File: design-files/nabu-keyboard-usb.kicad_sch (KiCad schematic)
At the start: 15 parts, among them J1 Console UART header, J2 DIN-6, J3 9V input, Q1 IRLU110PBF, U1 74LVC245, U2 Pico, U3 SN75176AP

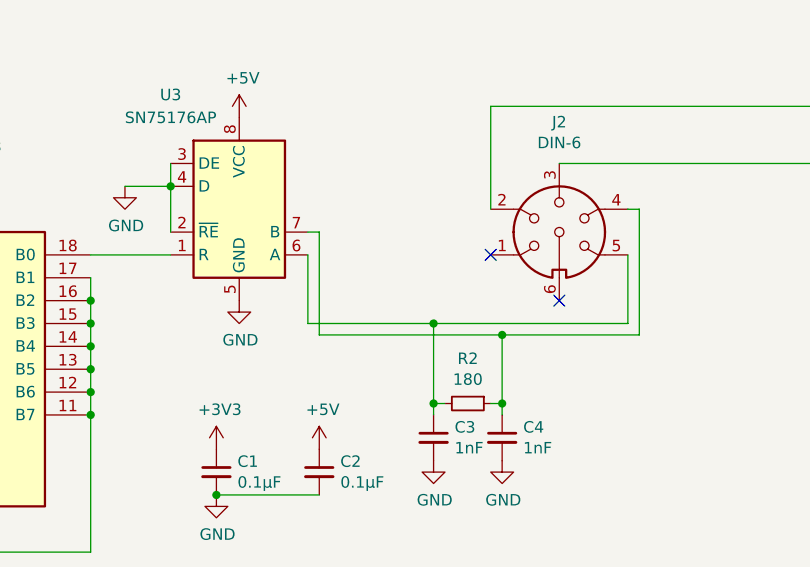
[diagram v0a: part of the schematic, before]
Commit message: Fix an error in the schematic that resulted in a non-working PCB; TX+ and TX- were swapped going into the 75176.
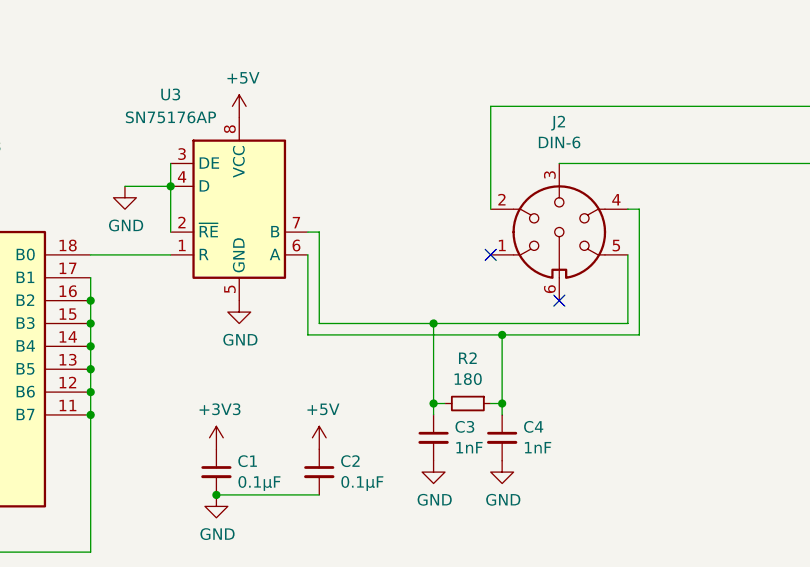
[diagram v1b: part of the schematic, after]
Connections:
- net at C3.1, J2.5, R2.2: now also U3.7 (B); no longer U3.6 (A)
- net at C4.1, J2.4, R2.1: now also U3.6 (A); no longer U3.7 (B)
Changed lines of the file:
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@@
   (title_block
     (title "NABU Keyboard to USB Adapter")
-    (date "2022-12-19")
-    (rev "0.1")
+    (date "2023-04-09")
+    (rev "0.2")
     (company "(c) 2022 Jason R. Thorpe. See LICENSE.")
   )
@@
   (junction (at 214.63 66.04) (diameter 0) (color 0 0 0 0)
   )
+  (junction (at 171.45 133.35) (diameter 0) (color 0 0 0 0)
+  )
   (junction (at 125.73 134.62) (diameter 0) (color 0 0 0 0)
   )
   (junction (at 125.73 129.54) (diameter 0) (color 0 0 0 0)
   )
-  (junction (at 171.45 133.35) (diameter 0) (color 0 0 0 0)
-  )
   (junction (at 125.73 142.24) (diameter 0) (color 0 0 0 0)
   )
@@
   (junction (at 121.92 81.28) (diameter 0) (color 0 0 0 0)
   )
+  (junction (at 121.92 55.88) (diameter 0) (color 0 0 0 0)
+  )
+  (junction (at 100.33 149.86) (diameter 0) (color 0 0 0 0)
+  )
+  (junction (at 163.83 140.97) (diameter 0) (color 0 0 0 0)
+  )
+  (junction (at 171.45 140.97) (diameter 0) (color 0 0 0 0)
+  )
+  (junction (at 207.01 60.96) (diameter 0) (color 0 0 0 0)
+  )
+  (junction (at 139.7 151.13) (diameter 0) (color 0 0 0 0)
+  )
   (junction (at 163.83 132.08) (diameter 0) (color 0 0 0 0)
-  )
-  (junction (at 121.92 55.88) (diameter 0) (color 0 0 0 0)
-  )
-  (junction (at 100.33 149.86) (diameter 0) (color 0 0 0 0)
-  )
-  (junction (at 163.83 140.97) (diameter 0) (color 0 0 0 0)
-  )
-  (junction (at 171.45 140.97) (diameter 0) (color 0 0 0 0)
-  )
-  (junction (at 207.01 60.96) (diameter 0) (color 0 0 0 0)
-  )
-  (junction (at 139.7 151.13) (diameter 0) (color 0 0 0 0)
   )
   (junction (at 134.62 116.84) (diameter 0) (color 0 0 0 0)
@@
     (stroke (width 0) (type default) (color 0 0 0 0))
   )
-  (wire (pts (xy 149.86 132.08) (xy 163.83 132.08))
-    (stroke (width 0) (type default) (color 0 0 0 0))
-  )
   (wire (pts (xy 125.73 137.16) (xy 125.73 139.7))
     (stroke (width 0) (type default) (color 0 0 0 0))
@@
     (stroke (width 0) (type default) (color 0 0 0 0))
   )
-  (wire (pts (xy 151.13 121.92) (xy 151.13 133.35))
-    (stroke (width 0) (type default) (color 0 0 0 0))
-  )
   (wire (pts (xy 106.68 38.1) (xy 124.46 38.1))
     (stroke (width 0) (type default) (color 0 0 0 0))
@@
     (stroke (width 0) (type default) (color 0 0 0 0))
   )
+  (wire (pts (xy 171.45 133.35) (xy 149.86 133.35))
+    (stroke (width 0) (type default) (color 0 0 0 0))
+  )
   (wire (pts (xy 185.42 132.08) (xy 185.42 124.46))
     (stroke (width 0) (type default) (color 0 0 0 0))
@@
     (stroke (width 0) (type default) (color 0 0 0 0))
   )
+  (wire (pts (xy 151.13 132.08) (xy 151.13 121.92))
+    (stroke (width 0) (type default) (color 0 0 0 0))
+  )
   (wire (pts (xy 160.02 68.58) (xy 162.56 68.58))
     (stroke (width 0) (type default) (color 0 0 0 0))
@@
     (stroke (width 0) (type default) (color 0 0 0 0))
   )
+  (wire (pts (xy 151.13 121.92) (xy 149.86 121.92))
+    (stroke (width 0) (type default) (color 0 0 0 0))
+  )
   (wire (pts (xy 223.52 114.3) (xy 177.8 114.3))
     (stroke (width 0) (type default) (color 0 0 0 0))
@@
     (stroke (width 0) (type default) (color 0 0 0 0))
   )
-  (wire (pts (xy 151.13 133.35) (xy 171.45 133.35))
-    (stroke (width 0) (type default) (color 0 0 0 0))
-  )
   (wire (pts (xy 106.68 40.64) (xy 124.46 40.64))
     (stroke (width 0) (type default) (color 0 0 0 0))
@@
     (stroke (width 0) (type default) (color 0 0 0 0))
   )
-  (wire (pts (xy 149.86 124.46) (xy 149.86 132.08))
-    (stroke (width 0) (type default) (color 0 0 0 0))
-  )
   (wire (pts (xy 134.62 114.3) (xy 134.62 116.84))
     (stroke (width 0) (type default) (color 0 0 0 0))
   )
+  (wire (pts (xy 163.83 132.08) (xy 151.13 132.08))
+    (stroke (width 0) (type default) (color 0 0 0 0))
+  )
   (wire (pts (xy 121.92 43.18) (xy 121.92 55.88))
     (stroke (width 0) (type default) (color 0 0 0 0))
@@
     (stroke (width 0) (type default) (color 0 0 0 0))
   )
-  (wire (pts (xy 149.86 121.92) (xy 151.13 121.92))
-    (stroke (width 0) (type default) (color 0 0 0 0))
-  )
+  (wire (pts (xy 149.86 133.35) (xy 149.86 124.46))
+    (stroke (width 0) (type default) (color 0 0 0 0))
+  )
